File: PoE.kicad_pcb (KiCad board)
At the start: 4 copper layers, 102.5 x 35 mm, 105 parts, among them J1 Conn_01x03, J1001 8P8C_LED_Shielded_x2, J1002 8P8C_LED_Shielded_x2, Q2 MMBT3906, Q2001 SI7898DP-T1-E3, U1 TPS563203, U1001 7490220122, U1002 TCMT1107, U2001 TPS23751PWP, U2002 TCMT1107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

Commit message: No change
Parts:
- moved U1 18.5 mm to (137.1, 43.8), turned to 90 degrees
- moved L1 0.61 mm to (131.2, 30.4)
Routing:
- net GNDREF: vias 78 -> 71
- added copper zone on In1.Cu, net +12V
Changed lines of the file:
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@@
 	(footprint "Package_TO_SOT_SMD:SOT-563"
 		(layer "F.Cu")
-		(at 130.5 26.5)
+		(at 137.1 43.8 90)
 		(descr "SOT563")
 		(tags "SOT-563")
 		(property "Reference" "U1"
-			(at 0 -1.9 0)
+			(at 0 -1.9 90)
 			(layer "F.SilkS")
 			(effects
@@
 		)
 		(property "Value" "TPS563203"
-			(at 0 1.75 0)
+			(at 0 1.75 90)
 			(layer "F.Fab")
 			(effects
@@
 		)
 		(property "Footprint" "Package_TO_SOT_SMD:SOT-563"
-			(at 0 0 0)
+			(at 0 0 90)
 			(unlocked yes)
 			(layer "F.Fab")
@@
 		)
 		(property "Datasheet" "https://www.ti.com/lit/ds/symlink/tps563203.pdf"
-			(at 0 0 0)
+			(at 0 0 90)
 			(unlocked yes)
 			(layer "F.Fab")
@@
 		)
 		(property "Description" "3A Synchronous Step-Down Voltage Regulator, Adjustable Output Voltage, 4.2-17V Input Voltage, 0.6-7V Output Voltage, Eco mode, SOT-563"
-			(at 0 0 0)
+			(at 0 0 90)
 			(unlocked yes)
 			(layer "F.Fab")
@@
 		(fp_line
 			(start -1.35 -1.1)
-			(end -1.35 1.1)
+			(end 1.35 -1.1)
 			(stroke
 				(width 0.05)
@@
 		(fp_line
 			(start -1.35 -1.1)
-			(end 1.35 -1.1)
+			(end -1.35 1.1)
 			(stroke
 				(width 0.05)
@@
 		(fp_line
 			(start 1.35 1.1)
-			(end -1.35 1.1)
+			(end 1.35 -1.1)
 			(stroke
 				(width 0.05)
@@
 		(fp_line
 			(start 1.35 1.1)
-			(end 1.35 -1.1)
+			(end -1.35 1.1)
 			(stroke
 				(width 0.05)
@@
 		)
 		(fp_line
-			(start -0.65 -0.5)
-			(end -0.65 0.85)
+			(start 0.65 -0.85)
+			(end -0.3 -0.85)
 			(stroke
 				(width 0.1)
@@
 		)
 		(fp_line
-			(start -0.65 0.85)
-			(end 0.65 0.85)
+			(start -0.65 -0.5)
+			(end -0.65 0.85)
 			(stroke
 				(width 0.1)
@@
 		)
 		(fp_line
-			(start 0.65 -0.85)
-			(end -0.3 -0.85)
+			(start 0.65 0.85)
+			(end 0.65 -0.85)
 			(stroke
 				(width 0.1)
@@
 		)
 		(fp_line
-			(start 0.65 0.85)
-			(end 0.65 -0.85)
+			(start -0.65 0.85)
+			(end 0.65 0.85)
 			(stroke
 				(width 0.1)
@@
 		)
 		(fp_text user "${REFERENCE}"
-			(at 0 0 90)
+			(at 0 0 360)
 			(layer "F.Fab")
 			(effects
@@
 		)
 		(pad "1" smd roundrect
-			(at -0.75 -0.5)
+			(at -0.75 -0.5 90)
 			(size 0.7 0.34)
 			(layers "F.Cu" "F.Paste" "F.Mask")
@@
 		)
 		(pad "2" smd roundrect
-			(at -0.75 0)
+			(at -0.75 0 90)
 			(size 0.7 0.34)
 			(layers "F.Cu" "F.Paste" "F.Mask")
@@
 		)
 		(pad "3" smd roundrect
-			(at -0.75 0.5)
+			(at -0.75 0.5 90)
 			(size 0.7 0.34)
 			(layers "F.Cu" "F.Paste" "F.Mask")
@@
 		)
 		(pad "4" smd roundrect
-			(at 0.75 0.5)
+			(at 0.75 0.5 90)
 			(size 0.7 0.34)
 			(layers "F.Cu" "F.Paste" "F.Mask")
@@
 		)
 		(pad "5" smd roundrect
-			(at 0.75 0)
+			(at 0.75 0 90)
 			(size 0.7 0.34)
 			(layers "F.Cu" "F.Paste" "F.Mask")
@@
 		)
 		(pad "6" smd roundrect
-			(at 0.75 -0.5)
+			(at 0.75 -0.5 90)
 			(size 0.7 0.34)
 			(layers "F.Cu" "F.Paste" "F.Mask")
@@
 	(footprint "Inductor_SMD:L_Abracon_ASPI-4030S"
 		(layer "F.Cu")
-		(at 130.6 30.3)
+		(at 131.2 30.4)
 		(descr "smd shielded power inductor 4x4x3mm, Abracon ASPI-4030S, https://abracon.com/Magnetics/power/ASPI-4030S.pdf")
 		(tags "inductor abracon smd shielded")
 		(property "Reference" "L1"
-			(at 0 -3 0)
+			(at 0 -3 360)
 			(layer "F.SilkS")
 			(effects
@@
 		)
 		(property "Value" "4.7u"
-			(at 0 3 0)
+			(at 0 3 360)
 			(layer "F.Fab")
 			(effects
@@
 		)
 		(fp_text user "${REFERENCE}"
-			(at 0 0 0)
+			(at 0 0 360)
 			(layer "F.Fab")
 			(effects
@@
 	)
 	(via
-		(at 124.5 40)
-		(size 0.25)
-		(drill 0.15)
-		(layers "F.Cu" "B.Cu")
-		(free yes)
-		(net 21)
-	)
-	(via
 		(at 139 57)
 		(size 0.25)
@@
 	)
 	(via
-		(at 124.5 31)
-		(size 0.25)
-		(drill 0.15)
-		(layers "F.Cu" "B.Cu")
-		(free yes)
-		(net 21)
-	)
-	(via
 		(at 144 28)
 		(size 0.25)
@@
 	)
 	(via
-		(at 124.5 36)
-		(size 0.25)
-		(drill 0.15)
-		(layers "F.Cu" "B.Cu")
-		(free yes)
-		(net 21)
-	)
-	(via
 		(at 135 57)
 		(size 0.25)
@@
 	)
 	(via
-		(at 124.5 28.5)
+		(at 97 42)
 		(size 0.25)
 		(drill 0.15)
@@
 	)
 	(via
-		(at 97 42)
+		(at 102.9 54.5)
 		(size 0.25)
 		(drill 0.15)
@@
 	)
 	(via
-		(at 102.9 54.5)
+		(at 95 44.6)
 		(size 0.25)
 		(drill 0.15)
 		(layers "F.Cu" "B.Cu")
-		(free yes)
 		(net 21)
 	)
@@
 	)
 	(via
-		(at 124.5 24)
-		(size 0.25)
-		(drill 0.15)
-		(layers "F.Cu" "B.Cu")
-		(free yes)
-		(net 21)
-	)
-	(via
 		(at 117 42)
 		(size 0.25)
@@
 	)
 	(via
-		(at 124.5 33.5)
-		(size 0.25)
-		(drill 0.15)
-		(layers "F.Cu" "B.Cu")
-		(free yes)
-		(net 21)
-	)
-	(via
 		(at 144 30)
 		(size 0.25)
@@
 	)
 	(via
-		(at 124.5 26)
-		(size 0.25)
-		(drill 0.15)
-		(layers "F.Cu" "B.Cu")
-		(free yes)
-		(net 21)
-	)
-	(via
 		(at 144 26)
 		(size 0.25)
@@
 	)
 	(via
-		(at 124.5 38)
-		(size 0.25)
-		(drill 0.15)
-		(layers "F.Cu" "B.Cu")
-		(free yes)
-		(net 21)
-	)
-	(via
 		(at 119 57)
 		(size 0.25)
@@
 		(net 80)
 		(net_name "+12V")
-		(layer "F.Cu")
+		(layers "F.Cu" "In1.Cu")
 		(hatch edge 0.5)
 		(priority 2)
@@
 		(polygon
 			(pts
-				(xy 110.9 44.2) (xy 134 44.2) (xy 134 48) (xy 110.9 48)
+				(xy 110.9 44.2) (xy 136.8 44.2) (xy 136.8 51.4) (xy 110.9 51.5)
 			)
 		)
@@
 		(polygon
 			(pts
-				(xy 63 39) (xy 63 23) (xy 124 23) (xy 124 41.5) (xy 94.5 41.5) (xy 94.5 26) (xy 82 26) (xy 82 39)
+				(xy 63 39) (xy 63 23) (xy 124.5 23) (xy 124.5 41.5) (xy 94.5 41.5) (xy 94.5 26) (xy 82 26) (xy 82 39)
 			)
 		)

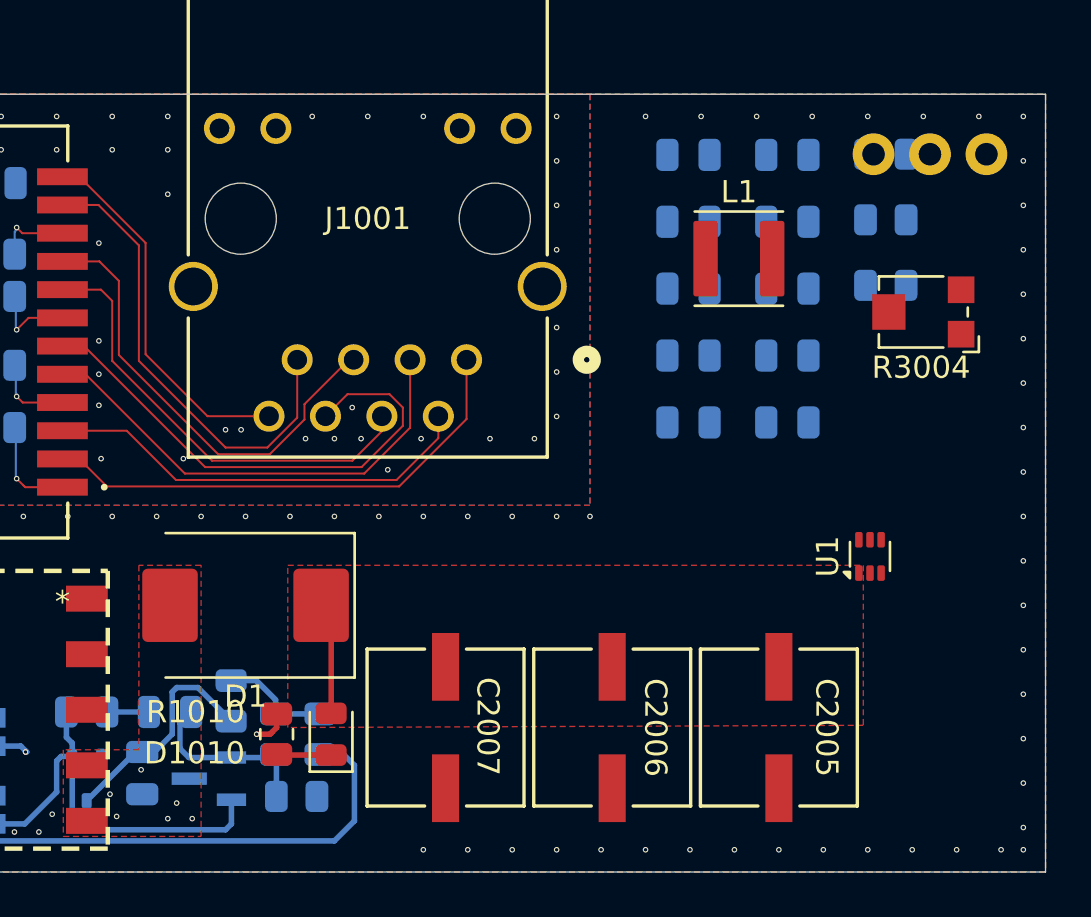
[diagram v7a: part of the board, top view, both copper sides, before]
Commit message: Added LEDs for status
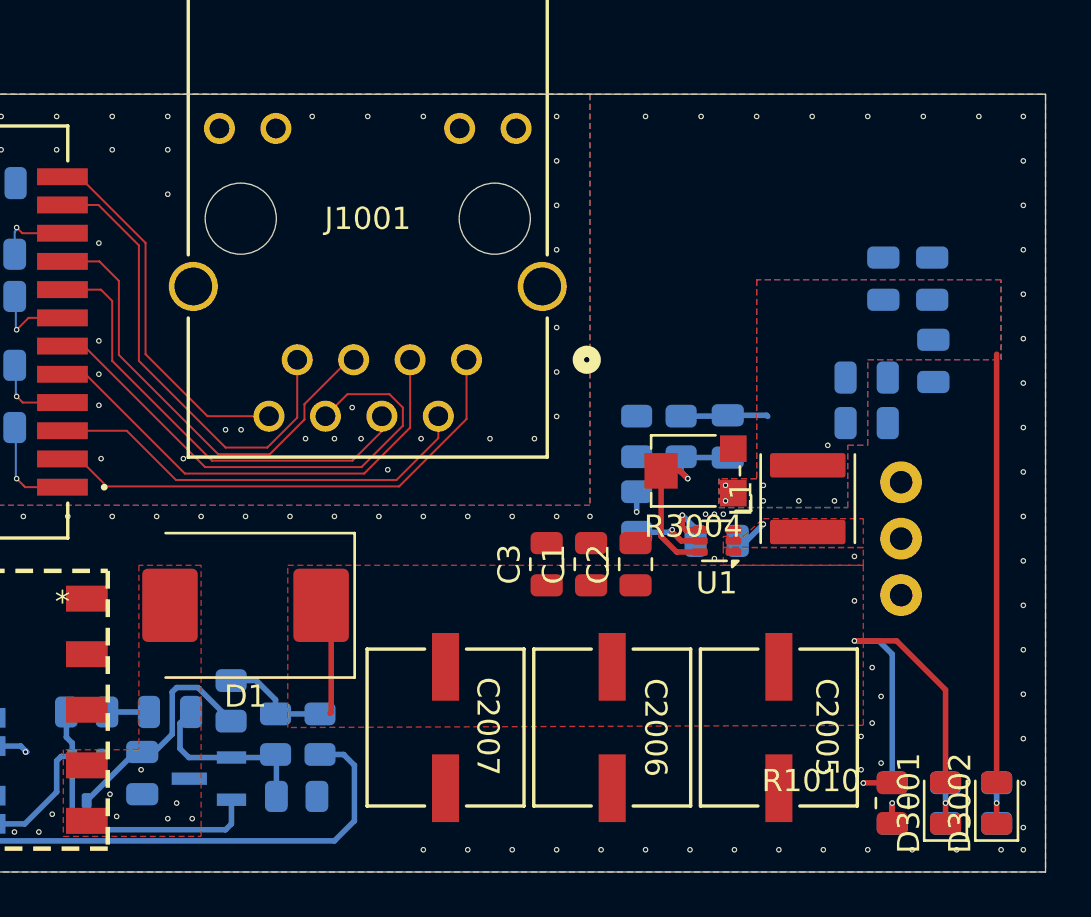
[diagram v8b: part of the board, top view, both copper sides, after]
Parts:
- added D3001: LED, LED_SMD:LED_0805_2012Metric, F.Cu at (140.5, 54.9)
- added D3002: LED, LED_SMD:LED_0805_2012Metric, F.Cu at (142.8, 54.9)
- added R3001: 10k, Resistor_SMD:R_0805_2012Metric, B.Cu at (140.5, 54.9)
- added R3002: 2.2k, Resistor_SMD:R_0805_2012Metric, B.Cu at (142.8, 54.9)
- C1, C2, C3: moved to F.Cu
- D1010: moved to B.Cu
- R1010: value 2.2k -> 10k
- moved R1010 27.9 mm to (138.1, 54.9)
- moved D1010 25.4 mm to (138.1, 54.9)
- moved C1 18.9 mm to (124.5, 44.1), turned to 90 degrees
- moved R2 16.9 mm to (126.6, 38.4), turned to -90 degrees
- moved C2 15.6 mm to (126.5, 44.1), turned to 90 degrees
- moved R4 15.2 mm to (126.6, 41.8), turned to -90 degrees
- moved J1 14.8 mm to (138.5, 40.5), turned to -90 degrees
- moved C3 13.9 mm to (122.5, 44.1), turned to 90 degrees
- moved R3 13.4 mm to (128.6, 38.4), turned to 90 degrees
- moved R3004 12.5 mm to (129.2, 40.0)
- moved L1 11.2 mm to (134.3, 41.2), turned to 90 degrees
- moved C6 10.6 mm to (136.9, 35.8), turned to 0 degrees
- moved C7 9.74 mm to (136.9, 37.8), turned to 0 degrees
- moved C4 8.44 mm to (130.2, 43.1)
- moved C10 7.78 mm to (137.7, 31.3), turned to 90 degrees
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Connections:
- net Net-(U1-SW) renamed /Output/SW
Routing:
- net Net-(R1010-Pad2): track 14.2 -> 42.1 mm
- net VOUT1: track 0.00 -> 23.2 mm, vias 0 -> 7
- net +12V: track 13.0 -> 32.1 mm, vias 0 -> 3
- net Net-(J1-Pin_2): track 0.00 -> 13.4 mm, vias 0 -> 1
- net Net-(U1-FB): track 0.00 -> 11.6 mm, vias 0 -> 1
- net Net-(U1-EN): track 0.00 -> 3.16 mm, vias 0 -> 1
- net Net-(U1-BST): track 0.00 -> 2.77 mm, vias 0 -> 1
- net Net-(D3002-K): track 0.00 -> 1.85 mm, vias 0 -> 1
- net Net-(D3001-K): track 0.00 -> 1.85 mm, vias 0 -> 1
- net /Output/SW: track 0.00 -> 1.46 mm, vias 0 -> 1
- net Net-(D1010-K): track 2.46 -> 1.85 mm, vias 0 -> 1
- net GNDREF: vias 71 -> 81
- added copper zone on F.Cu, net /Output/SW
- added copper zone on B.Cu, net VOUT1
- added copper zone on F.Cu, net VOUT1
